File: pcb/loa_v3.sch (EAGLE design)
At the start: 111 parts, among them IC1 STM32F10XVXT6, IC2 M25P80MW, IC3 S34ML04G100TFI000, IC4 MCP1825S-1202E/DB, IC5 NCP3170, IC6 AD7265SU, Q2 50.000, Q3 25.000, U1 6SLX9TQG144, X3 MINI-USB

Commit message: Fixed DP and DM naming for USB
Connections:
- net USB_D+: now also JP3.3, R13.2, X3G$1.3; no longer JP3.2, R12.2, X3G$1.2
- net USB_D-: now also JP3.2, R12.2, X3G$1.2; no longer JP3.3, R13.2, X3G$1.3
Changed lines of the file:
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@@
 <?xml version="1.0" encoding="utf-8"?>
 <!DOCTYPE eagle SYSTEM "eagle.dtd">
-<eagle version="6.5.0">
+<eagle version="6.4">
 <drawing>
 <settings>
@@
 <grid distance="0.1" unitdist="inch" unit="inch" style="lines" multiple="1" display="no" altdistance="0.01" altunitdist="inch" altunit="inch"/>
 <layers>
-<layer number="1" name="Top" color="4" fill="1" visible="yes" active="no"/>
-<layer number="2" name="Route2" color="1" fill="3" visible="yes" active="no"/>
-<layer number="3" name="Route3" color="11" fill="1" visible="yes" active="no"/>
-<layer number="4" name="Route4" color="1" fill="4" visible="yes" active="no"/>
-<layer number="5" name="Route5" color="4" fill="4" visible="yes" active="no"/>
-<layer number="6" name="Route6" color="1" fill="8" visible="yes" active="no"/>
-<layer number="7" name="Route7" color="4" fill="8" visible="yes" active="no"/>
-<layer number="8" name="Route8" color="1" fill="2" visible="yes" active="no"/>
-<layer number="9" name="Route9" color="4" fill="2" visible="yes" active="no"/>
-<layer number="10" name="Route10" color="1" fill="7" visible="yes" active="no"/>
-<layer number="11" name="Route11" color="4" fill="7" visible="yes" active="no"/>
-<layer number="12" name="Route12" color="1" fill="5" visible="yes" active="no"/>
-<layer number="13" name="Route13" color="4" fill="5" visible="yes" active="no"/>
-<layer number="14" name="Route14" color="1" fill="6" visible="yes" active="no"/>
-<layer number="15" name="Route15" color="11" fill="6" visible="yes" active="no"/>
-<layer number="16" name="Bottom" color="1" fill="1" visible="yes" active="no"/>
-<layer number="17" name="Pads" color="2" fill="1" visible="yes" active="no"/>
-<layer number="18" name="Vias" color="2" fill="1" visible="yes" active="no"/>
-<layer number="19" name="Unrouted" color="6" fill="1" visible="yes" active="no"/>
-<layer number="20" name="Dimension" color="15" fill="1" visible="yes" active="no"/>
-<layer number="21" name="tPlace" color="7" fill="1" visible="yes" active="no"/>
-<layer number="22" name="bPlace" color="7" fill="1" visible="yes" active="no"/>
-<layer number="23" name="tOrigins" color="15" fill="1" visible="yes" active="no"/>
-<layer number="24" name="bOrigins" color="15" fill="1" visible="yes" active="no"/>
-<layer number="25" name="tNames" color="7" fill="1" visible="yes" active="no"/>
-<layer number="26" name="bNames" color="7" fill="1" visible="yes" active="no"/>
-<layer number="27" name="tValues" color="7" fill="1" visible="yes" active="no"/>
-<layer number="28" name="bValues" color="7" fill="1" visible="yes" active="no"/>
+<layer number="1" name="Top" color="4" fill="1" visible="no" active="no"/>
+<layer number="2" name="Route2" color="1" fill="3" visible="no" active="no"/>
+<layer number="3" name="Route3" color="11" fill="1" visible="no" active="no"/>
+<layer number="4" name="Route4" color="1" fill="4" visible="no" active="no"/>
+<layer number="5" name="Route5" color="4" fill="4" visible="no" active="no"/>
+<layer number="6" name="Route6" color="1" fill="8" visible="no" active="no"/>
+<layer number="7" name="Route7" color="4" fill="8" visible="no" active="no"/>
+<layer number="8" name="Route8" color="1" fill="2" visible="no" active="no"/>
+<layer number="9" name="Route9" color="4" fill="2" visible="no" active="no"/>
+<layer number="10" name="Route10" color="1" fill="7" visible="no" active="no"/>
+<layer number="11" name="Route11" color="4" fill="7" visible="no" active="no"/>
+<layer number="12" name="Route12" color="1" fill="5" visible="no" active="no"/>
+<layer number="13" name="Route13" color="4" fill="5" visible="no" active="no"/>
+<layer number="14" name="Route14" color="1" fill="6" visible="no" active="no"/>
+<layer number="15" name="Route15" color="11" fill="6" visible="no" active="no"/>
+<layer number="16" name="Bottom" color="1" fill="1" visible="no" active="no"/>
+<layer number="17" name="Pads" color="2" fill="1" visible="no" active="no"/>
+<layer number="18" name="Vias" color="2" fill="1" visible="no" active="no"/>
+<layer number="19" name="Unrouted" color="6" fill="1" visible="no" active="no"/>
+<layer number="20" name="Dimension" color="15" fill="1" visible="no" active="no"/>
+<layer number="21" name="tPlace" color="7" fill="1" visible="no" active="no"/>
+<layer number="22" name="bPlace" color="7" fill="1" visible="no" active="no"/>
+<layer number="23" name="tOrigins" color="15" fill="1" visible="no" active="no"/>
+<layer number="24" name="bOrigins" color="15" fill="1" visible="no" active="no"/>
+<layer number="25" name="tNames" color="7" fill="1" visible="no" active="no"/>
+<layer number="26" name="bNames" color="7" fill="1" visible="no" active="no"/>
+<layer number="27" name="tValues" color="7" fill="1" visible="no" active="no"/>
+<layer number="28" name="bValues" color="7" fill="1" visible="no" active="no"/>
 <layer number="29" name="tStop" color="7" fill="3" visible="no" active="no"/>
 <layer number="30" name="bStop" color="7" fill="6" visible="no" active="no"/>
@@
 <layer number="35" name="tGlue" color="7" fill="4" visible="no" active="no"/>
 <layer number="36" name="bGlue" color="7" fill="5" visible="no" active="no"/>
-<layer number="37" name="tTest" color="7" fill="1" visible="yes" active="no"/>
-<layer number="38" name="bTest" color="7" fill="1" visible="yes" active="no"/>
+<layer number="37" name="tTest" color="7" fill="1" visible="no" active="no"/>
+<layer number="38" name="bTest" color="7" fill="1" visible="no" active="no"/>
 <layer number="39" name="tKeepout" color="4" fill="11" visible="no" active="no"/>
 <layer number="40" name="bKeepout" color="1" fill="11" visible="no" active="no"/>
@@
 <layer number="44" name="Drills" color="7" fill="1" visible="no" active="no"/>
 <layer number="45" name="Holes" color="7" fill="1" visible="no" active="no"/>
-<layer number="46" name="Milling" color="3" fill="1" visible="yes" active="no"/>
-<layer number="47" name="Measures" color="7" fill="1" visible="yes" active="no"/>
-<layer number="48" name="Document" color="7" fill="1" visible="yes" active="no"/>
-<layer number="49" name="Reference" color="7" fill="1" visible="yes" active="no"/>
-<layer number="50" name="dxf" color="7" fill="1" visible="yes" active="no"/>
-<layer number="51" name="tDocu" color="7" fill="1" visible="yes" active="no"/>
-<layer number="52" name="bDocu" color="7" fill="1" visible="yes" active="no"/>
-<layer number="53" name="tGND_GNDA" color="7" fill="9" visible="yes" active="no"/>
-<layer number="54" name="bGND_GNDA" color="1" fill="9" visible="yes" active="no"/>
-<layer number="56" name="wert" color="7" fill="1" visible="yes" active="no"/>
+<layer number="46" name="Milling" color="3" fill="1" visible="no" active="no"/>
+<layer number="47" name="Measures" color="7" fill="1" visible="no" active="no"/>
+<layer number="48" name="Document" color="7" fill="1" visible="no" active="no"/>
+<layer number="49" name="Reference" color="7" fill="1" visible="no" active="no"/>
+<layer number="50" name="dxf" color="7" fill="1" visible="no" active="no"/>
+<layer number="51" name="tDocu" color="7" fill="1" visible="no" active="no"/>
+<layer number="52" name="bDocu" color="7" fill="1" visible="no" active="no"/>
+<layer number="53" name="tGND_GNDA" color="7" fill="9" visible="no" active="no"/>
+<layer number="54" name="bGND_GNDA" color="1" fill="9" visible="no" active="no"/>
+<layer number="56" name="wert" color="7" fill="1" visible="no" active="no"/>
 <layer number="91" name="Nets" color="2" fill="1" visible="yes" active="yes"/>
 <layer number="92" name="Busses" color="1" fill="1" visible="yes" active="yes"/>
@@
 </segment>
 </net>
-<net name="USB_D-" class="0">
+<net name="USB_D+" class="0">
 <segment>
 <pinref part="JP3" gate="A" pin="3"/>
@@
 </segment>
 </net>
-<net name="USB_D+" class="0">
+<net name="USB_D-" class="0">
 <segment>
 <pinref part="JP3" gate="A" pin="2"/>
@@
 </segment>
 </net>
-<net name="USB_D-" class="0">
+<net name="USB_D+" class="0">
 <segment>
 <wire x1="215.9" y1="71.12" x2="220.98" y2="71.12" width="0.1524" layer="91"/>
@@
 </segment>
 </net>
-<net name="USB_D+" class="0">
+<net name="USB_D-" class="0">
 <segment>
 <wire x1="215.9" y1="73.66" x2="218.44" y2="73.66" width="0.1524" layer="91"/>

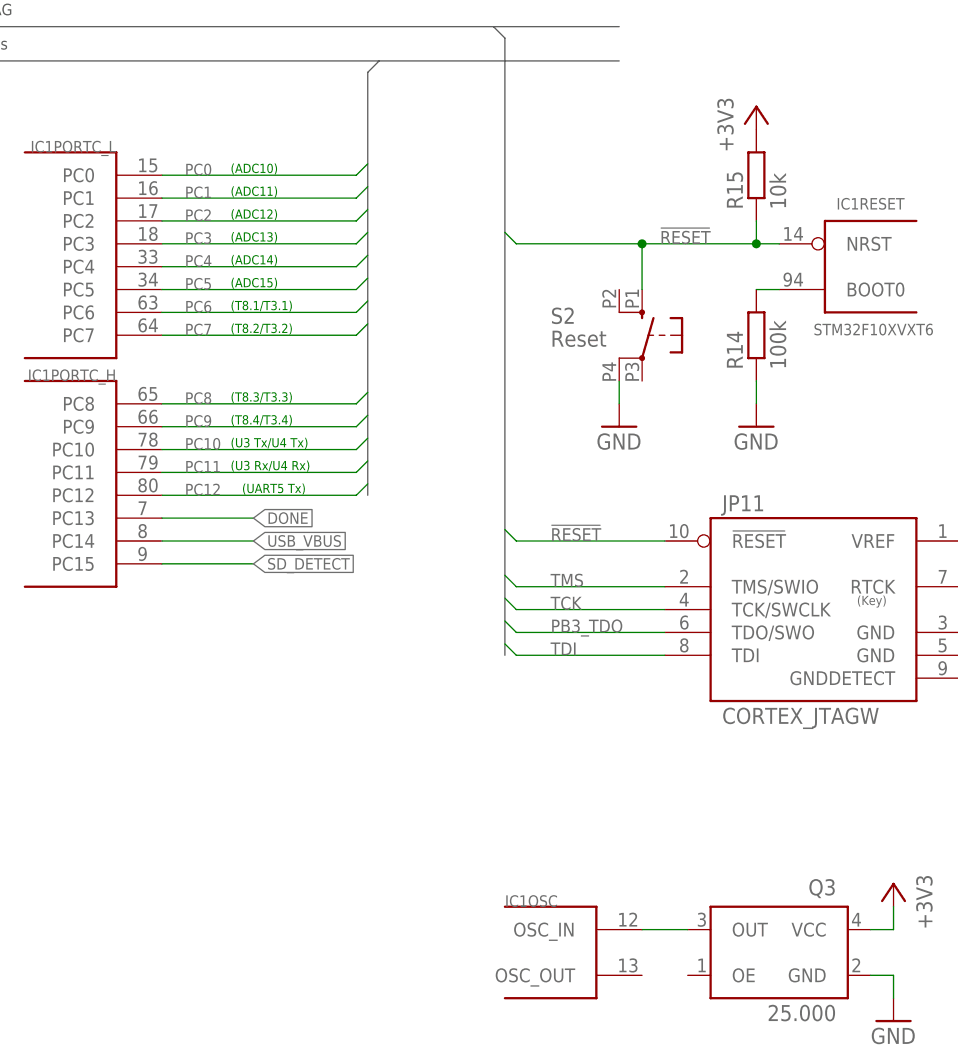
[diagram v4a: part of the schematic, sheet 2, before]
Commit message: Voltage divider added for the V_USB sense pin
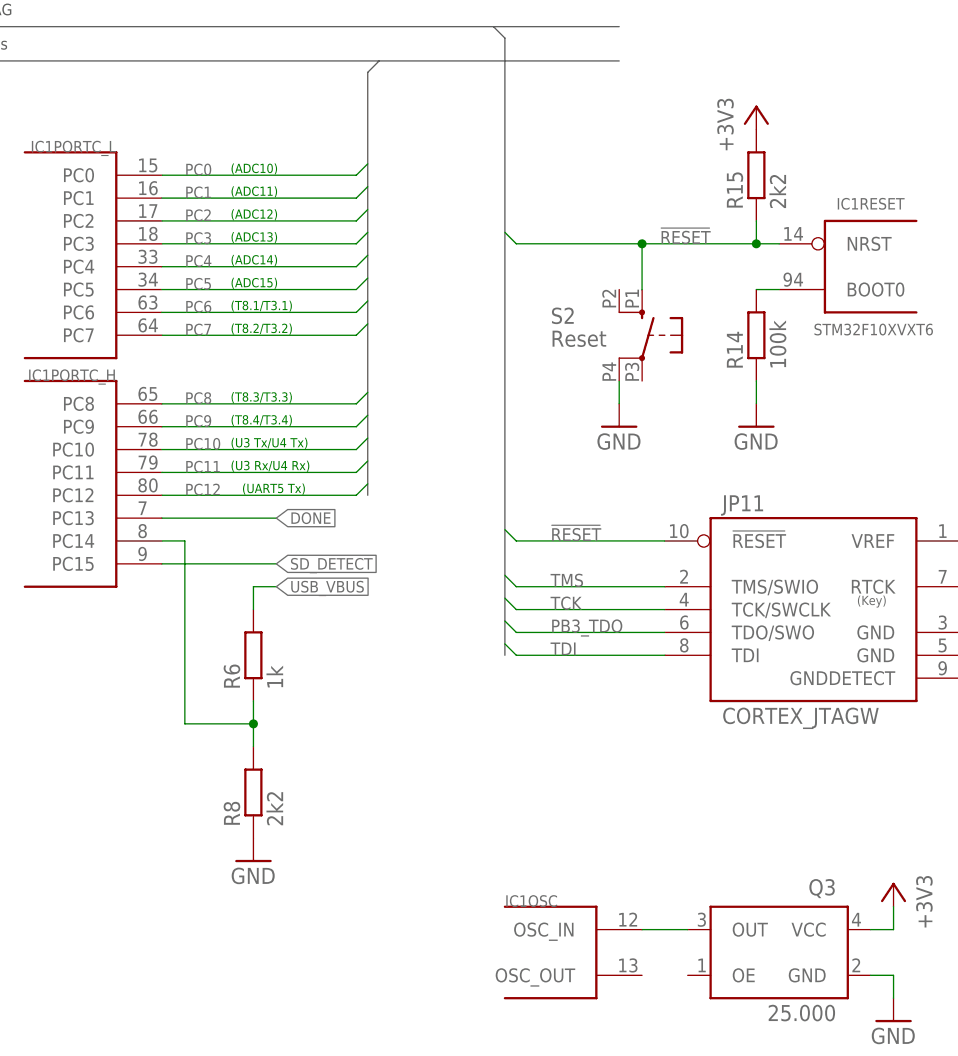
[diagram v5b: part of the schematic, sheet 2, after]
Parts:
- added R6: 1k, rcl:R-EU_R0603
- added R8: 2k2, rcl:R-EU_R0603
- R15: value 10k -> 2k2
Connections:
- new net N$19: IC1PORTC_H.PC14, R6.1, R8.2
- net GND: now also R8.1
- net USB_VBUS: now also R6.2; no longer IC1PORTC_H.PC14
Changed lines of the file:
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@@
 <?xml version="1.0" encoding="utf-8"?>
 <!DOCTYPE eagle SYSTEM "eagle.dtd">
-<eagle version="6.4">
+<eagle version="6.5.0">
 <drawing>
 <settings>
@@
 <part name="R14" library="rcl" deviceset="R-EU_" device="R0603" value="100k"/>
 <part name="GND72" library="supply1" deviceset="GND" device=""/>
-<part name="R15" library="rcl" deviceset="R-EU_" device="R0603" value="10k"/>
+<part name="R15" library="rcl" deviceset="R-EU_" device="R0603" value="2k2"/>
 <part name="+3V16" library="supply1" deviceset="+3V3" device=""/>
 <part name="Q3" library="rca_sontiges" deviceset="XO" device="53" value="25.000">
@@
 <part name="JP8" library="pinhead2" deviceset="PINHD-1X1" device="_2.54" value="GND"/>
 <part name="GND24" library="supply1" deviceset="GND" device=""/>
+<part name="R6" library="rcl" deviceset="R-EU_" device="R0603" value="1k"/>
+<part name="R8" library="rcl" deviceset="R-EU_" device="R0603" value="2k2"/>
+<part name="GND27" library="supply1" deviceset="GND" device=""/>
 </parts>
 <sheets>
@@
 <attribute name="REICHELT#" x="226.06" y="76.2" size="1.778" layer="96" display="off"/>
 </instance>
+<instance part="R6" gate="G$1" x="165.1" y="71.12" rot="R90"/>
+<instance part="R8" gate="G$1" x="165.1" y="55.88" rot="R90"/>
+<instance part="GND27" gate="1" x="165.1" y="48.26"/>
 </instances>
 <busses>
@@
 <pinref part="GND8" gate="1" pin="GND"/>
 </segment>
+<segment>
+<pinref part="R8" gate="G$1" pin="1"/>
+<pinref part="GND27" gate="1" pin="GND"/>
+</segment>
 </net>
 <net name="!RESET" class="0">
@@
 <net name="SD_DETECT" class="0">
 <segment>
-<wire x1="154.94" y1="81.28" x2="165.1" y2="81.28" width="0.1524" layer="91"/>
-<label x="165.1" y="81.28" size="1.27" layer="95" xref="yes"/>
+<wire x1="154.94" y1="81.28" x2="167.64" y2="81.28" width="0.1524" layer="91"/>
+<label x="167.64" y="81.28" size="1.27" layer="95" xref="yes"/>
 <pinref part="IC1" gate="PORTC_H" pin="PC15"/>
 </segment>
@@
 <net name="USB_VBUS" class="0">
 <segment>
-<wire x1="154.94" y1="83.82" x2="165.1" y2="83.82" width="0.1524" layer="91"/>
-<label x="165.1" y="83.82" size="1.27" layer="95" xref="yes"/>
-<pinref part="IC1" gate="PORTC_H" pin="PC14"/>
+<label x="167.64" y="78.74" size="1.27" layer="95" xref="yes"/>
+<wire x1="165.1" y1="76.2" x2="165.1" y2="78.74" width="0.1524" layer="91"/>
+<wire x1="165.1" y1="78.74" x2="167.64" y2="78.74" width="0.1524" layer="91"/>
+<pinref part="R6" gate="G$1" pin="2"/>
 </segment>
 </net>
 <net name="DONE" class="0">
 <segment>
-<wire x1="154.94" y1="86.36" x2="165.1" y2="86.36" width="0.1524" layer="91"/>
-<label x="165.1" y="86.36" size="1.27" layer="95" xref="yes"/>
+<wire x1="154.94" y1="86.36" x2="167.64" y2="86.36" width="0.1524" layer="91"/>
+<label x="167.64" y="86.36" size="1.27" layer="95" xref="yes"/>
 <pinref part="IC1" gate="PORTC_H" pin="PC13"/>
 </segment>
@@
 </segment>
 </net>
+<net name="N$19" class="0">
+<segment>
+<pinref part="R8" gate="G$1" pin="2"/>
+<pinref part="R6" gate="G$1" pin="1"/>
+<wire x1="165.1" y1="60.96" x2="165.1" y2="63.5" width="0.1524" layer="91"/>
+<wire x1="165.1" y1="63.5" x2="165.1" y2="66.04" width="0.1524" layer="91"/>
+<wire x1="165.1" y1="63.5" x2="157.48" y2="63.5" width="0.1524" layer="91"/>
+<junction x="165.1" y="63.5"/>
+<pinref part="IC1" gate="PORTC_H" pin="PC14"/>
+<wire x1="157.48" y1="63.5" x2="157.48" y2="83.82" width="0.1524" layer="91"/>
+<wire x1="157.48" y1="83.82" x2="154.94" y2="83.82" width="0.1524" layer="91"/>
+</segment>
+</net>
